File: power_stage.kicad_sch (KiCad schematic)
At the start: 27 parts, among them J1 Input, J1 Output, Q1 IMW120R014M1H, Q2 IMW120R014M1H, Q6 2N7002BK,215, U4 TC4432VOA

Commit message: design update
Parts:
- removed C17: 4.7nF, Capacitor_SMD:C_1812_4532Metric, symbol Device:C
- added C2: 4.7nF, Capacitor_SMD:C_1812_4532Metric, symbol Device:C
- added D8, D9: D, Diode_THT:D_DO-201AE_P12.70mm_Horizontal, symbol Device:D
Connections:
- net VSOURCE: now also R26.2, R27.2, D8.1 (K), D9.1 (K)
- net at R26.1: now also C2.2, D9.2 (A)
- net at R27.1: now also C16.2, D8.2 (A); no longer R26.2
- net at J1.1, J1.2, J1.3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: no longer R27.2
- net at Q2.2 (D), R3.1, RV1.2: now also C16.1
- net at J1.1, J1.2, J1.3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: now also C2.1; no longer C16.1
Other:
- moved on the sheet: J1, RV1

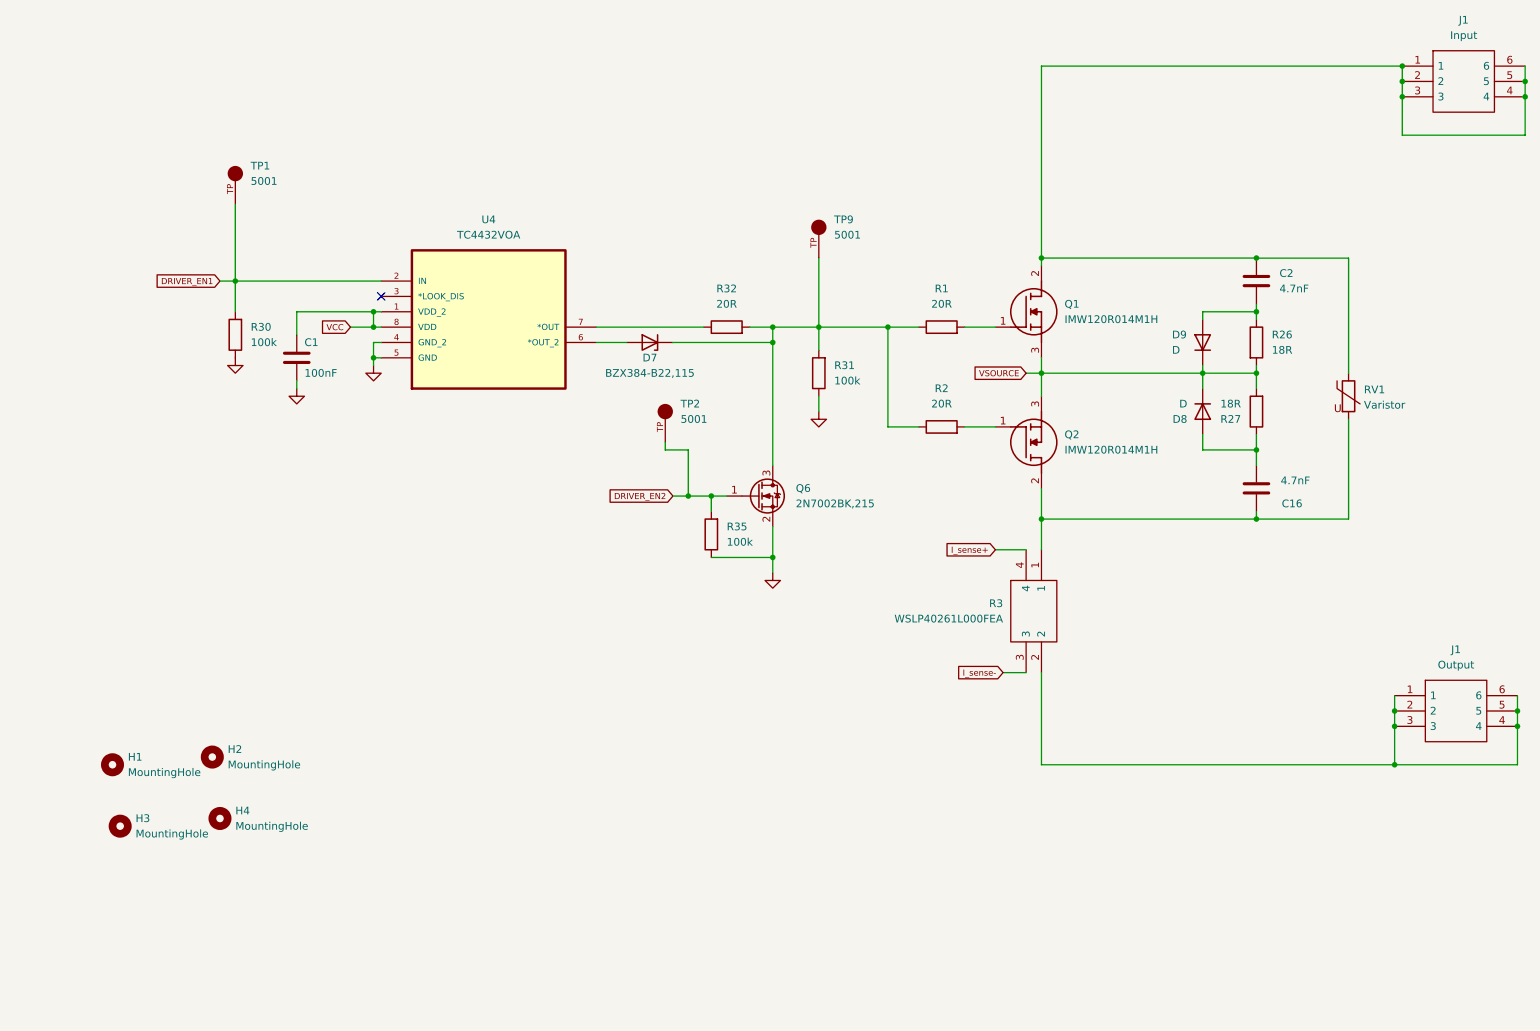
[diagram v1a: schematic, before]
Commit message: Design with footprint error
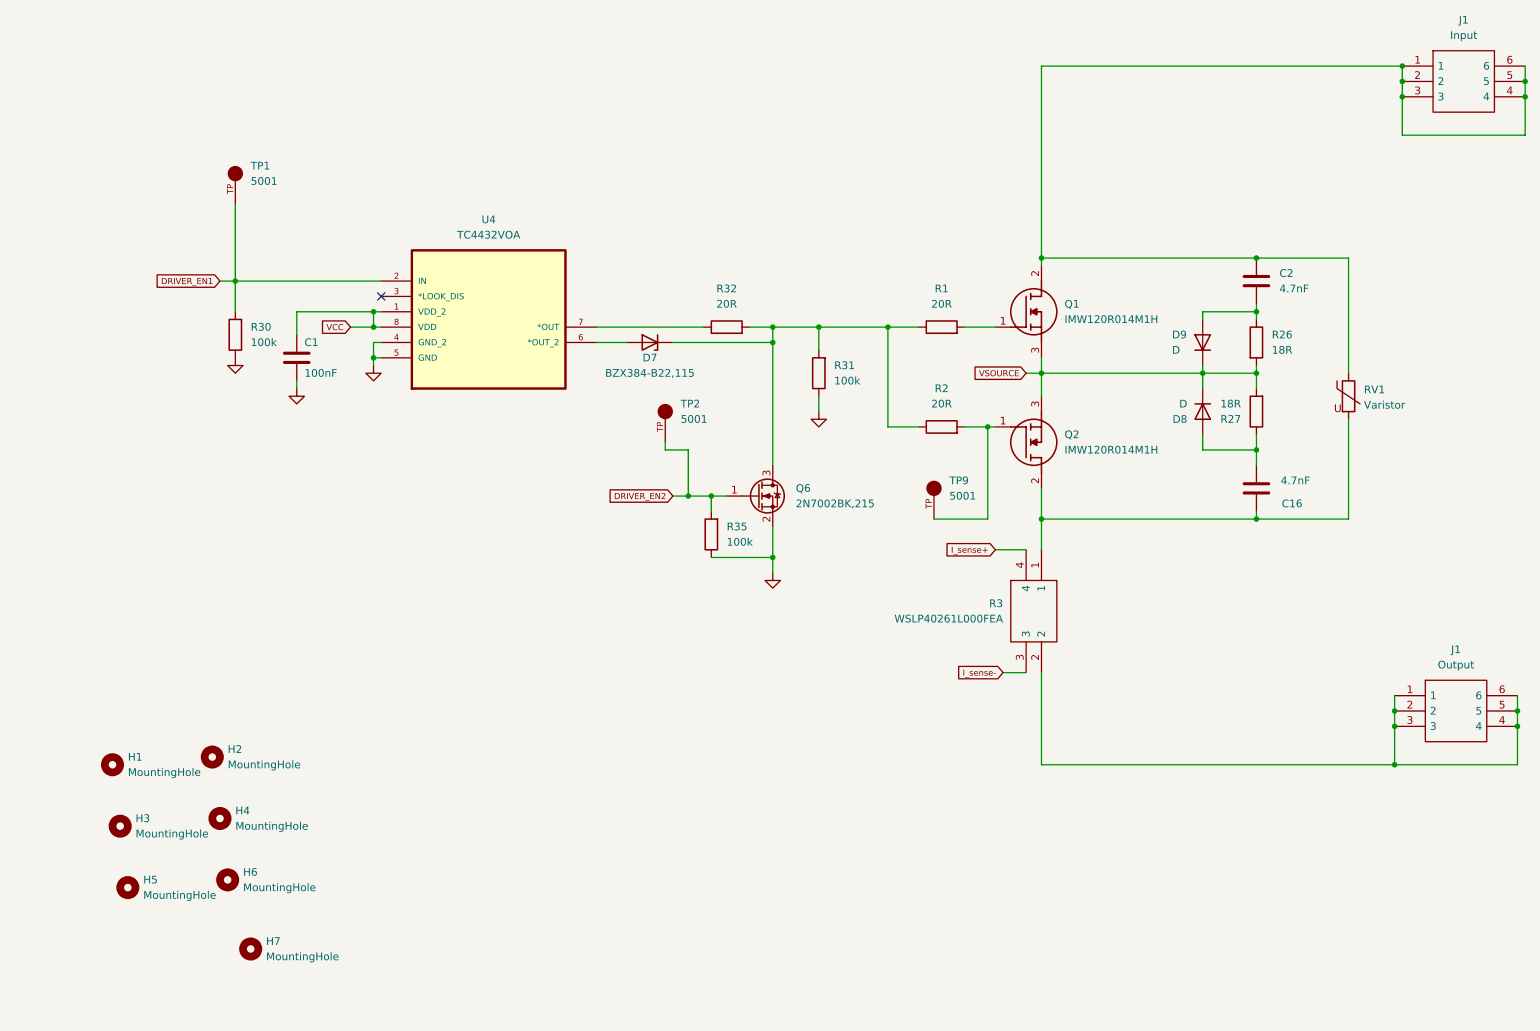
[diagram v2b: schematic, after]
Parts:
- added H5, H6, H7: MountingHole, MountingHole:MountingHole_3.2mm_M3, symbol Mechanical:MountingHole
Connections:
- net at D7.1 (K), Q6.3 (D), R1.1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: no longer TP9.TP
- net at Q2.1 (G), R2.2: now also TP9.TP
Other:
- moved on the sheet: TP9
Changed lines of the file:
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@@
   (junction (at 273.05 39.37) (diameter 0) (color 0 0 0 0)
+  )
+  (junction (at 184.15 93.98) (diameter 0) (color 0 0 0 0)
   )
   (junction (at 228.6 74.93) (diameter 0) (color 0 0 0 0)
@@
     (stroke (width 0) (type default))
   )
-  (wire (pts (xy 185.42 93.98) (xy 180.34 93.98))
-    (stroke (width 0) (type default))
-  )
   (wire (pts (xy 219.71 97.79) (xy 219.71 95.25))
     (stroke (width 0) (type default))
@@
     (stroke (width 0) (type default))
   )
+  (wire (pts (xy 184.15 93.98) (xy 180.34 93.98))
+    (stroke (width 0) (type default))
+  )
   (wire (pts (xy 132.08 105.41) (xy 134.62 105.41))
     (stroke (width 0) (type default))
@@
     (stroke (width 0) (type default))
   )
+  (wire (pts (xy 184.15 93.98) (xy 185.42 93.98))
+    (stroke (width 0) (type default))
+  )
   (wire (pts (xy 271.78 143.51) (xy 271.78 149.86))
     (stroke (width 0) (type default))
@@
     (stroke (width 0) (type default))
   )
+  (wire (pts (xy 184.15 109.22) (xy 184.15 93.98))
+    (stroke (width 0) (type default))
+  )
+  (wire (pts (xy 184.15 109.22) (xy 175.26 109.22))
+    (stroke (width 0) (type default))
+  )
   (wire (pts (xy 193.04 34.29) (xy 193.04 66.04))
     (stroke (width 0) (type default))
@@
   )
   (wire (pts (xy 156.21 91.44) (xy 156.21 88.9))
-    (stroke (width 0) (type default))
-  )
-  (wire (pts (xy 156.21 66.04) (xy 156.21 77.47))
     (stroke (width 0) (type default))
   )
@@
     )
   )
+  (symbol (lib_id "Mechanical:MountingHole") (at 62.23 180.34 0) (unit 1)
+    (in_bom yes) (on_board yes) (dnp no) (fields_autoplaced)
+    (property "Reference" "H7" (at 64.77 179.07 0)
+      (effects (font (size 1.27 1.27)) (justify left))
+    )
+    (property "Value" "MountingHole" (at 64.77 181.61 0)
+      (effects (font (size 1.27 1.27)) (justify left))
+    )
+    (property "Footprint" "MountingHole:MountingHole_3.2mm_M3" (at 62.23 180.34 0)
+      (effects (font (size 1.27 1.27)) hide)
+    )
+    (property "Datasheet" "~" (at 62.23 180.34 0)
+      (effects (font (size 1.27 1.27)) hide)
+    )
+    (instances
+      (project "SiC based Battery Disconnect"
+        (path "/525387b1-1528-4728-a616-6f57d2a34d69/a4af0f90-9694-45a8-86a1-2f9082dd6b02"
+          (reference "H7") (unit 1)
+        )
+      )
+    )
+  )
   (symbol (lib_id "5001:5001") (at 130.81 91.44 90) (unit 1)
     (in_bom yes) (on_board yes) (dnp no) (fields_autoplaced)
@@
     )
   )
+  (symbol (lib_id "Mechanical:MountingHole") (at 58.42 168.91 0) (unit 1)
+    (in_bom yes) (on_board yes) (dnp no) (fields_autoplaced)
+    (property "Reference" "H6" (at 60.96 167.64 0)
+      (effects (font (size 1.27 1.27)) (justify left))
+    )
+    (property "Value" "MountingHole" (at 60.96 170.18 0)
+      (effects (font (size 1.27 1.27)) (justify left))
+    )
+    (property "Footprint" "MountingHole:MountingHole_3.2mm_M3" (at 58.42 168.91 0)
+      (effects (font (size 1.27 1.27)) hide)
+    )
+    (property "Datasheet" "~" (at 58.42 168.91 0)
+      (effects (font (size 1.27 1.27)) hide)
+    )
+    (instances
+      (project "SiC based Battery Disconnect"
+        (path "/525387b1-1528-4728-a616-6f57d2a34d69/a4af0f90-9694-45a8-86a1-2f9082dd6b02"
+          (reference "H6") (unit 1)
+        )
+      )
+    )
+  )
   (symbol (lib_id "7461057:7461057") (at 251.46 138.43 0) (unit 1)
     (in_bom yes) (on_board yes) (dnp no) (fields_autoplaced)
@@
     )
   )
-  (symbol (lib_id "5001:5001") (at 156.21 60.96 90) (unit 1)
-    (in_bom yes) (on_board yes) (dnp no) (fields_autoplaced)
-    (property "Reference" "TP9" (at 158.75 59.69 90)
+  (symbol (lib_id "5001:5001") (at 175.26 104.14 90) (unit 1)
+    (in_bom yes) (on_board yes) (dnp no) (fields_autoplaced)
+    (property "Reference" "TP9" (at 177.8 102.87 90)
       (effects (font (size 1.27 1.27)) (justify right))
     )
-    (property "Value" "5001" (at 158.75 62.23 90)
+    (property "Value" "5001" (at 177.8 105.41 90)
       (effects (font (size 1.27 1.27)) (justify right))
     )
-    (property "Footprint" "5001 tp:KEYSTONE_5001" (at 156.21 60.96 0)
-      (effects (font (size 1.27 1.27)) (justify bottom) hide)
-    )
-    (property "Datasheet" "" (at 156.21 60.96 0)
-      (effects (font (size 1.27 1.27)) hide)
-    )
-    (property "MF" "Keystone Electronics Corp." (at 156.21 60.96 0)
-      (effects (font (size 1.27 1.27)) (justify bottom) hide)
-    )
-    (property "MAXIMUM_PACKAGE_HEIGHT" "4.57 mm" (at 156.21 60.96 0)
-      (effects (font (size 1.27 1.27)) (justify bottom) hide)
-    )
-    (property "Package" "None" (at 156.21 60.96 0)
-      (effects (font (size 1.27 1.27)) (justify bottom) hide)
-    )
-    (property "Price" "None" (at 156.21 60.96 0)
-      (effects (font (size 1.27 1.27)) (justify bottom) hide)
-    )
-    (property "Check_prices" "https://www.snapeda.com/parts/5001/Keystone+Electronics/view-part/?ref=eda" (at 156.21 60.96 0)
-      (effects (font (size 1.27 1.27)) (justify bottom) hide)
-    )
-    (property "STANDARD" "Manufacturer Recommendations" (at 156.21 60.96 0)
-      (effects (font (size 1.27 1.27)) (justify bottom) hide)
-    )
-    (property "PARTREV" "H" (at 156.21 60.96 0)
-      (effects (font (size 1.27 1.27)) (justify bottom) hide)
-    )
-    (property "SnapEDA_Link" "https://www.snapeda.com/parts/5001/Keystone+Electronics/view-part/?ref=snap" (at 156.21 60.96 0)
-      (effects (font (size 1.27 1.27)) (justify bottom) hide)
-    )
-    (property "MP" "5001" (at 156.21 60.96 0)
-      (effects (font (size 1.27 1.27)) (justify bottom) hide)
-    )
-    (property "Description" "\nBlack PC Test Point, Miniature Phosphor Bronze Silver Plating 0.040 (1.02mm) Hole Diameter Mounting Type\n" (at 156.21 60.96 0)
-      (effects (font (size 1.27 1.27)) (justify bottom) hide)
-    )
-    (property "MANUFACTURER" "Keystone" (at 156.21 60.96 0)
-      (effects (font (size 1.27 1.27)) (justify bottom) hide)
-    )
-    (property "Availability" "In Stock" (at 156.21 60.96 0)
-      (effects (font (size 1.27 1.27)) (justify bottom) hide)
-    )
-    (property "SNAPEDA_PN" "5000" (at 156.21 60.96 0)
+    (property "Footprint" "5001 tp:KEYSTONE_5001" (at 175.26 104.14 0)
+      (effects (font (size 1.27 1.27)) (justify bottom) hide)
+    )
+    (property "Datasheet" "" (at 175.26 104.14 0)
+      (effects (font (size 1.27 1.27)) hide)
+    )
+    (property "MF" "Keystone Electronics Corp." (at 175.26 104.14 0)
+      (effects (font (size 1.27 1.27)) (justify bottom) hide)
+    )
+    (property "MAXIMUM_PACKAGE_HEIGHT" "4.57 mm" (at 175.26 104.14 0)
+      (effects (font (size 1.27 1.27)) (justify bottom) hide)
+    )
+    (property "Package" "None" (at 175.26 104.14 0)
+      (effects (font (size 1.27 1.27)) (justify bottom) hide)
+    )
+    (property "Price" "None" (at 175.26 104.14 0)
+      (effects (font (size 1.27 1.27)) (justify bottom) hide)
+    )
+    (property "Check_prices" "https://www.snapeda.com/parts/5001/Keystone+Electronics/view-part/?ref=eda" (at 175.26 104.14 0)
+      (effects (font (size 1.27 1.27)) (justify bottom) hide)
+    )
+    (property "STANDARD" "Manufacturer Recommendations" (at 175.26 104.14 0)
+      (effects (font (size 1.27 1.27)) (justify bottom) hide)
+    )
+    (property "PARTREV" "H" (at 175.26 104.14 0)
+      (effects (font (size 1.27 1.27)) (justify bottom) hide)
+    )
+    (property "SnapEDA_Link" "https://www.snapeda.com/parts/5001/Keystone+Electronics/view-part/?ref=snap" (at 175.26 104.14 0)
+      (effects (font (size 1.27 1.27)) (justify bottom) hide)
+    )
+    (property "MP" "5001" (at 175.26 104.14 0)
+      (effects (font (size 1.27 1.27)) (justify bottom) hide)
+    )
+    (property "Description" "\nBlack PC Test Point, Miniature Phosphor Bronze Silver Plating 0.040 (1.02mm) Hole Diameter Mounting Type\n" (at 175.26 104.14 0)
+      (effects (font (size 1.27 1.27)) (justify bottom) hide)
+    )
+    (property "MANUFACTURER" "Keystone" (at 175.26 104.14 0)
+      (effects (font (size 1.27 1.27)) (justify bottom) hide)
+    )
+    (property "Availability" "In Stock" (at 175.26 104.14 0)
+      (effects (font (size 1.27 1.27)) (justify bottom) hide)
+    )
+    (property "SNAPEDA_PN" "5000" (at 175.26 104.14 0)
       (effects (font (size 1.27 1.27)) (justify bottom) hide)
     )
@@
         )
       )
+    )
+  )
+  (symbol (lib_id "Mechanical:MountingHole") (at 41.91 170.18 0) (unit 1)
+    (in_bom yes) (on_board yes) (dnp no) (fields_autoplaced)
+    (property "Reference" "H5" (at 44.45 168.91 0)
+      (effects (font (size 1.27 1.27)) (justify left))
+    )
+    (property "Value" "MountingHole" (at 44.45 171.45 0)
+      (effects (font (size 1.27 1.27)) (justify left))
+    )
+    (property "Footprint" "MountingHole:MountingHole_3.2mm_M3" (at 41.91 170.18 0)
+      (effects (font (size 1.27 1.27)) hide)
+    )
+    (property "Datasheet" "~" (at 41.91 170.18 0)
+      (effects (font (size 1.27 1.27)) hide)
+    )
+    (instances
+      (project "SiC based Battery Disconnect"
+        (path "/525387b1-1528-4728-a616-6f57d2a34d69/a4af0f90-9694-45a8-86a1-2f9082dd6b02"
+          (reference "H5") (unit 1)
+        )
+      )

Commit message: Final Design
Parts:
- RV1: value Varistor -> MOV
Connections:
- net Vgate: now reaches D7.1 (K), Q6.3 (D), R1.1, R2.1, R31.2, R32.2
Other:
- moved on the sheet: C1, C16, C2, D7, D8, D9, H1, H2, H3, H4, H5, H6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
